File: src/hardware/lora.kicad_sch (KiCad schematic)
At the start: 19 parts, among them IC1 LLCC68IMLTRT, U21 TPS22916BYFPR, U22 0900FM15K0039001E, U23 BGS12WN6E6327XTSA1, Y4 NSC5359C-32M

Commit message: Changed footprints from 0603 to 0402
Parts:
- C57, C58, C59, C60, C61, C62, C63, C64, C65: footprint Capacitor_SMD:C_0603_1608Metric -> Capacitor_SMD:C_0504_1310Metric
- R32, R33: footprint Resistor_SMD:R_0603_1608Metric -> Resistor_SMD:R_0402_1005Metric
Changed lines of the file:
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@@
 			)
 		)
-		(property "Footprint" "Capacitor_SMD:C_0603_1608Metric"
+		(property "Footprint" "Capacitor_SMD:C_0504_1310Metric"
 			(at 136.8552 105.41 0)
 			(effects
@@
 			)
 		)
-		(property "Footprint" "Capacitor_SMD:C_0603_1608Metric"
+		(property "Footprint" "Capacitor_SMD:C_0504_1310Metric"
 			(at 104.14 67.6148 0)
 			(effects
@@
 			)
 		)
-		(property "Footprint" "Resistor_SMD:R_0603_1608Metric"
+		(property "Footprint" "Resistor_SMD:R_0402_1005Metric"
 			(at 66.548 127 90)
 			(effects
@@
 			)
 		)
-		(property "Footprint" "Capacitor_SMD:C_0603_1608Metric"
+		(property "Footprint" "Capacitor_SMD:C_0504_1310Metric"
 			(at 53.0352 128.27 0)
 			(effects
@@
 			)
 		)
-		(property "Footprint" "Capacitor_SMD:C_0603_1608Metric"
+		(property "Footprint" "Capacitor_SMD:C_0504_1310Metric"
 			(at 107.95 91.7448 0)
 			(effects
@@
 			)
 		)
-		(property "Footprint" "Resistor_SMD:R_0603_1608Metric"
+		(property "Footprint" "Resistor_SMD:R_0402_1005Metric"
 			(at 115.57 70.358 90)
 			(effects
@@
 			)
 		)
-		(property "Footprint" "Capacitor_SMD:C_0603_1608Metric"
+		(property "Footprint" "Capacitor_SMD:C_0504_1310Metric"
 			(at 225.0948 116.84 0)
 			(effects
@@
 			)
 		)
-		(property "Footprint" "Capacitor_SMD:C_0603_1608Metric"
+		(property "Footprint" "Capacitor_SMD:C_0504_1310Metric"
 			(at 105.1052 66.04 0)
 			(effects
@@
 			)
 		)
-		(property "Footprint" "Capacitor_SMD:C_0603_1608Metric"
+		(property "Footprint" "Capacitor_SMD:C_0504_1310Metric"
 			(at 125.4252 105.41 0)
 			(effects
@@
 			)
 		)
-		(property "Footprint" "Capacitor_SMD:C_0603_1608Metric"
+		(property "Footprint" "Capacitor_SMD:C_0504_1310Metric"
 			(at 234.95 129.8448 0)
 			(effects
@@
 			)
 		)
-		(property "Footprint" "Capacitor_SMD:C_0603_1608Metric"
+		(property "Footprint" "Capacitor_SMD:C_0504_1310Metric"
 			(at 49.8348 109.22 0)
 			(effects

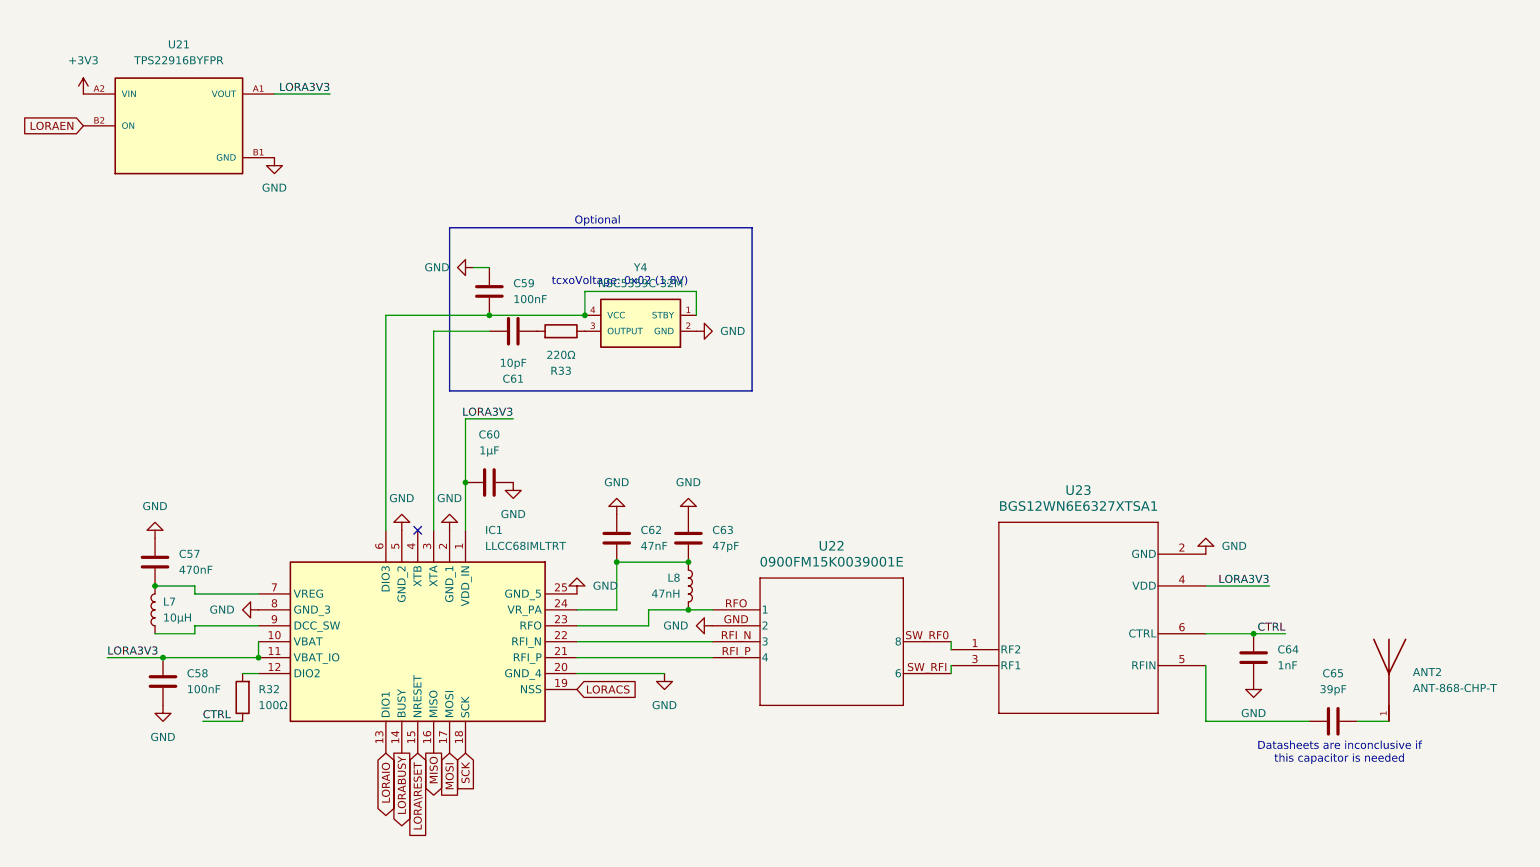
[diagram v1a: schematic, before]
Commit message: Replaced global labels with pin headers
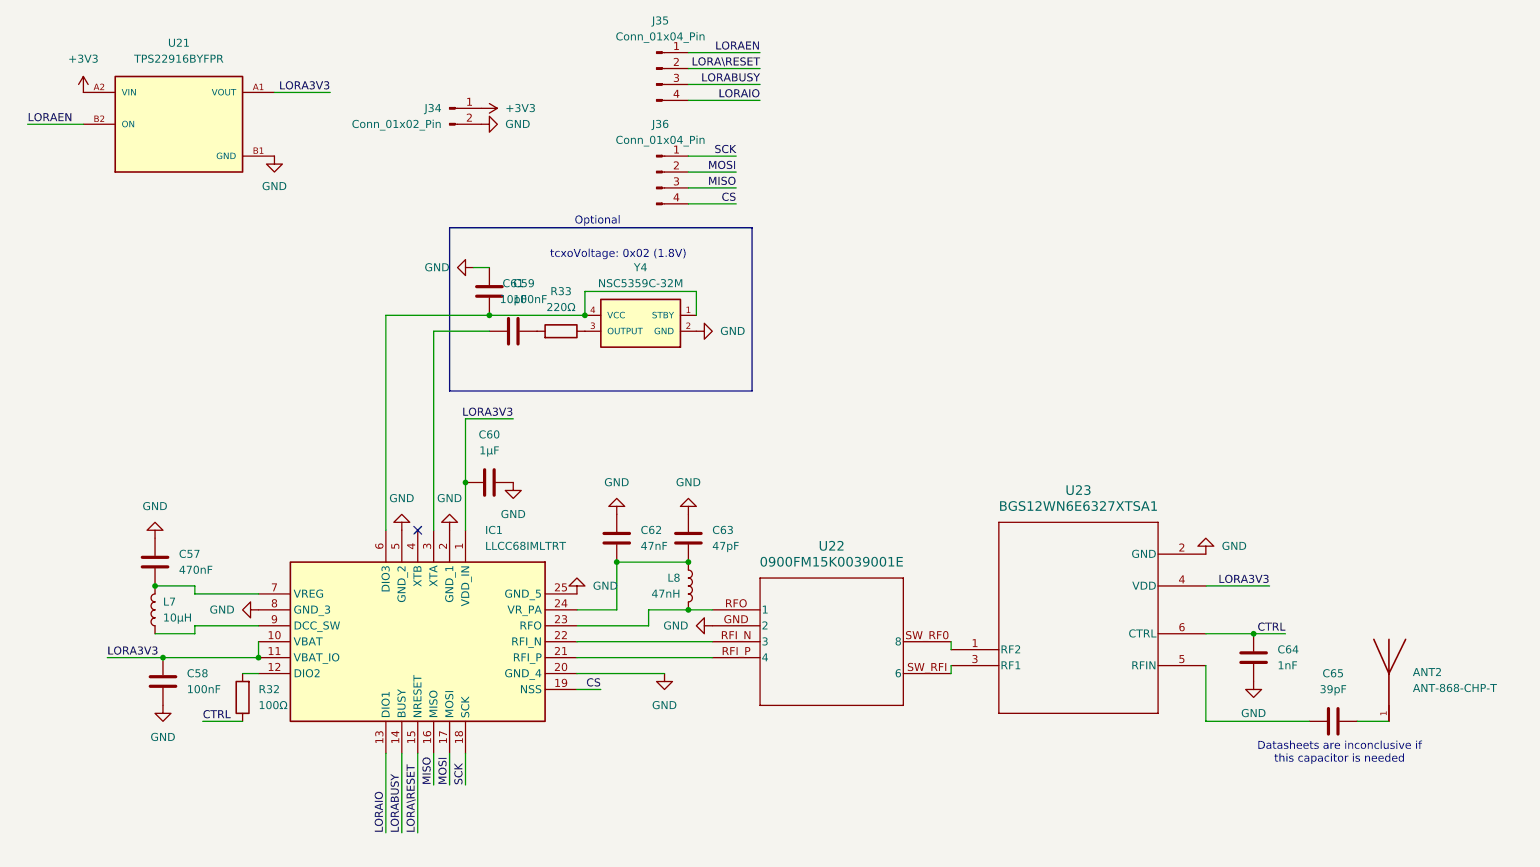
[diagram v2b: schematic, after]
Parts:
- added J34: Conn_01x02_Pin, symbol Connector:Conn_01x02_Pin
- added J35, J36: Conn_01x04_Pin, symbol Connector:Conn_01x04_Pin
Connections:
- net +3V3: now also J34.1 (Pin_1)
- net GND: now also J34.2 (Pin_2)
- net LORABUSY: now also J35.3 (Pin_3)
- net LORAEN: now also J35.1 (Pin_1)
- net LORAIO: now also J35.4 (Pin_4)
- net LORA\RESET: now also J35.2 (Pin_2)
- net MISO: now also J36.3 (Pin_3)
- net MOSI: now also J36.2 (Pin_2)
- net SCK: now also J36.1 (Pin_1)
- net LORACS renamed CS
- net CS: now also J36.4 (Pin_4)

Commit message: Reannotated schematic
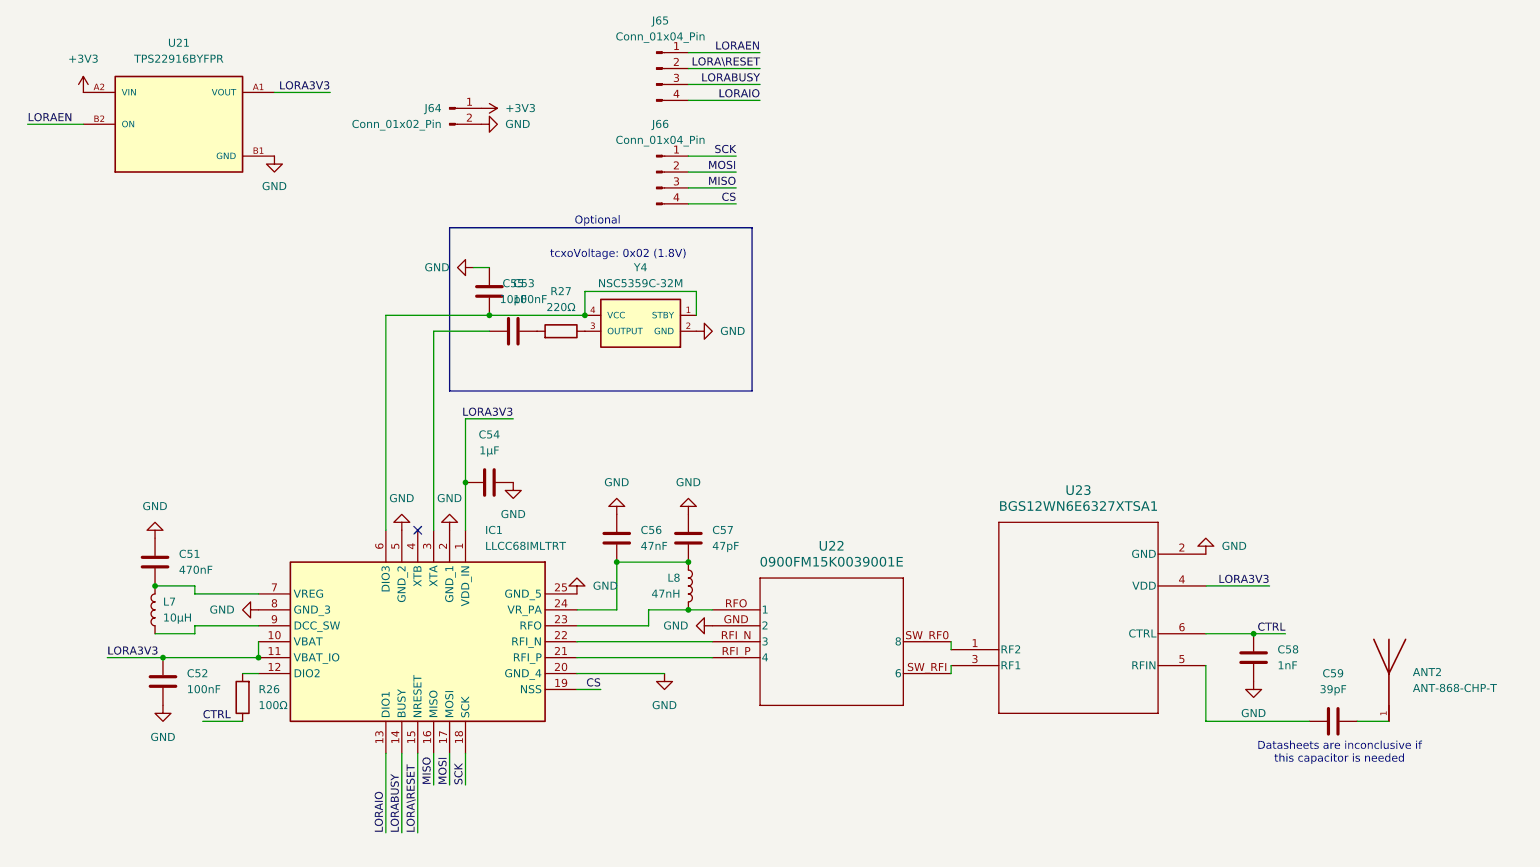
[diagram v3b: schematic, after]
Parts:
- renumbered C57 to C51, C58 to C52, C59 to C53, C60 to C54, C61 to C55, C62 to C56, C63 to C57, C64 to C58, C65 to C59, J34 to J64, J35 to J65, J36 to J66, R32 to R26, R33 to R27

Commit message: Assigned pin header footprints
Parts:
- J64: footprint (none) -> Connector_PinHeader_2.54mm:PinHeader_1x02_P2.54mm_Horizontal
- J65, J66: footprint (none) -> Connector_PinHeader_2.54mm:PinHeader_1x04_P2.54mm_Horizontal
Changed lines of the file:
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@@
 			)
 		)
-		(property "Footprint" ""
+		(property "Footprint" "Connector_PinHeader_2.54mm:PinHeader_1x04_P2.54mm_Horizontal"
 			(at 130.81 43.18 0)
 			(effects
@@
 			)
 		)
-		(property "Footprint" ""
+		(property "Footprint" "Connector_PinHeader_2.54mm:PinHeader_1x04_P2.54mm_Horizontal"
 			(at 130.81 26.67 0)
 			(effects
@@
 			)
 		)
-		(property "Footprint" ""
+		(property "Footprint" "Connector_PinHeader_2.54mm:PinHeader_1x02_P2.54mm_Horizontal"
 			(at 97.79 33.02 0)
 			(effects

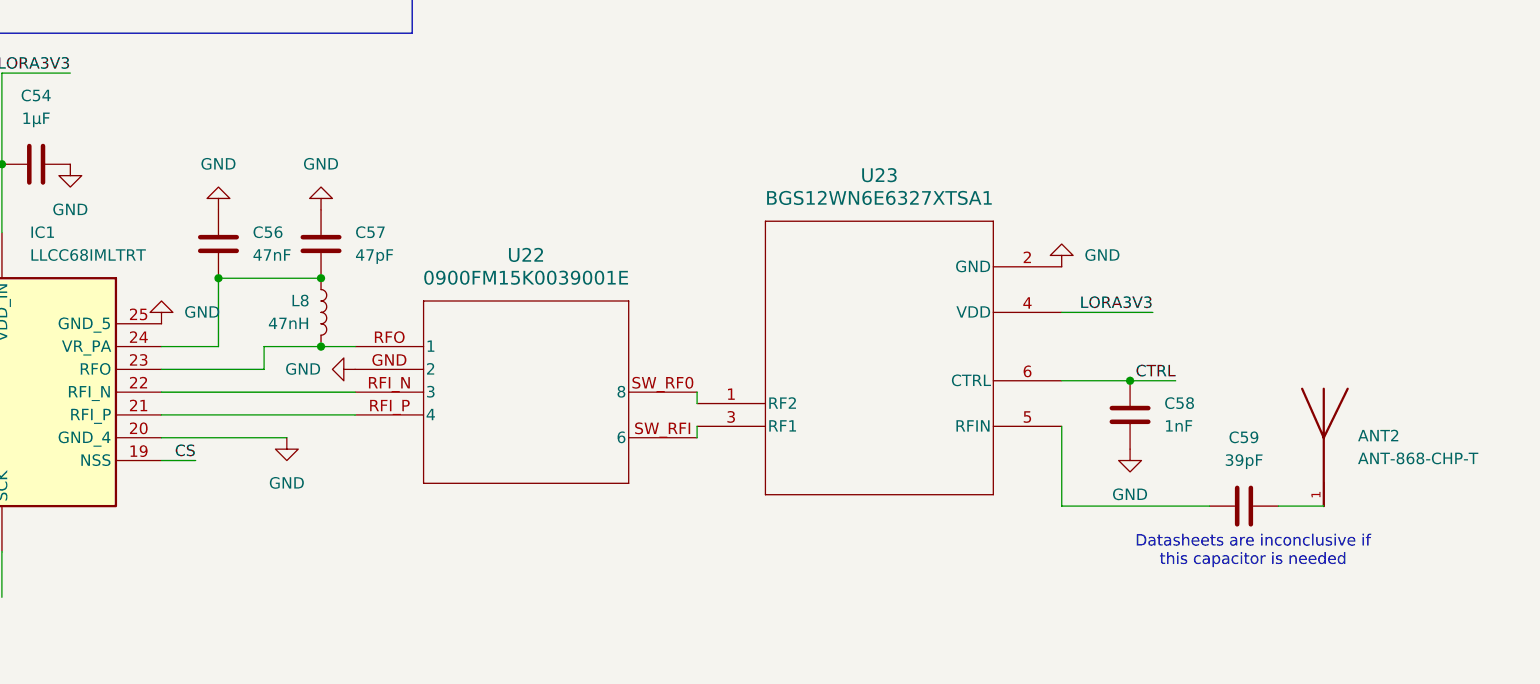
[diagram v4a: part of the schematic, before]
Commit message: Fixed 0900FM15K0039001E symbol
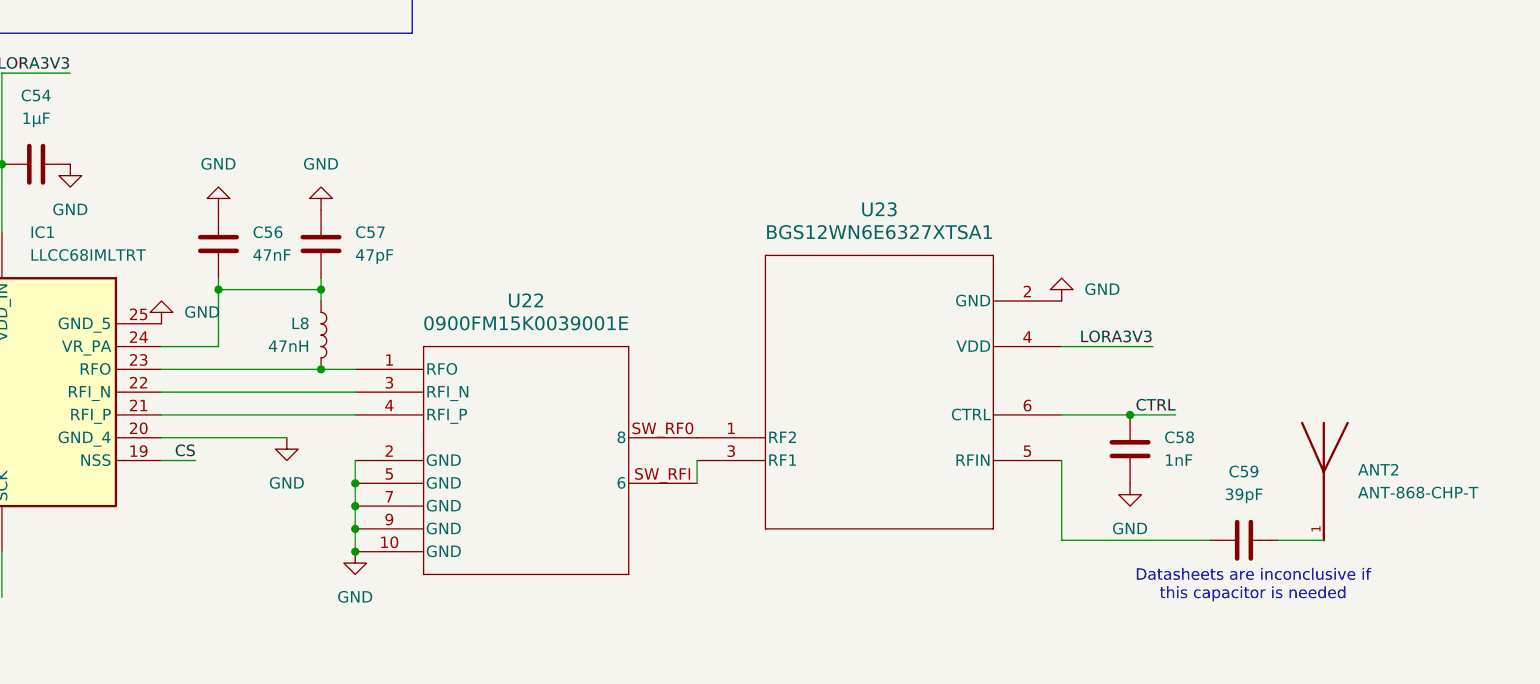
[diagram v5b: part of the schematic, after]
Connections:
- net GND: now also U22.10 (GND), U22.2 (GND), U22.5 (GND), U22.7 (GND), U22.9 (GND); no longer U22.GND (2)
- net at IC1.22 (RFI_N): now also U22.3 (RFI_N); no longer U22.RFI_N (3)
- net at IC1.21 (RFI_P): now also U22.4 (RFI_P); no longer U22.RFI_P (4)
- net at IC1.23 (RFO), L8.2: now also U22.1 (RFO); no longer U22.RFO (1)
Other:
- moved on the sheet: ANT2, C58, C59, L8, U23

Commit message: Fixed 0900FM15K0039001E symbol
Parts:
- U22: footprint Project:QFP20P0X0X31-0_JOT -> QFP20P0X0X31-0_JOT
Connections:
- net at U23.1 (RF2): now also U22.8 (SW_RFO); no longer U22.SW_RF0 (8)
- net at U23.3 (RF1): now also U22.6 (SW_RFI); no longer U22.SW_RFI (6)
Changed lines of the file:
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@@
-	(wire
-		(pts
-			(xy 177.8 128.27) (xy 177.8 125.73)
-		)
-		(stroke
-			(width 0)
-			(type default)
-		)
-	)
 	(wire
 		(pts
@@
 			)
 		)
-		(property "Footprint" "Project:QFP20P0X0X31-0_JOT"
+		(property "Footprint" "QFP20P0X0X31-0_JOT"
 			(at 139.7 118.11 0)
 			(effects
@@
 		(pin "3"
 		)
-		(pin "SW_RF0"
+		(pin "8"
 		)
 		(pin "4"
@@
 		(pin "2"
 		)
-		(pin "SW_RFI"
+		(pin "6"
 		)
 		(pin "9"

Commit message: Fixed ANT1 Footprint
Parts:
- renumbered IC1 to U?
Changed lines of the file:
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@@
 		(dnp no)
 		(fields_autoplaced yes)
-		(property "Reference" "IC1"
+		(property "Reference" "U?"
 			(at 103.4481 100.33 90)
 			(effects
@@
 			(project "raywatch"
 				(path "/7b654ee8-2a53-4d39-8b7d-32c7bb3cb0ed/500b48f3-f083-4626-a865-624bdd615c7c"
-					(reference "IC1")
+					(reference "U?")
 					(unit 1)
 				)

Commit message: Fixed ANT2
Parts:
- ANT2: footprint Project:XTAL_ABS07-32.768KHZ-7-T -> ANT-868-CHP-T:XDCR_ANT-868-CHP-T
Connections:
- net GND: now also ANT2.2 (GND)
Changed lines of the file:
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@@
+	)
+	(symbol
+		(lib_id "power:GND")
+		(at 247.65 113.03 180)
+		(unit 1)
+		(exclude_from_sim no)
+		(in_bom yes)
+		(on_board yes)
+		(dnp no)
+		(fields_autoplaced yes)
+		(property "Reference" "#PWR0497"
+			(at 247.65 106.68 0)
+			(effects
+				(font
+					(size 1.27 1.27)
+				)
+				(hide yes)
+			)
+		)
+		(property "Value" "GND"
+			(at 247.65 107.95 0)
+			(effects
+				(font
+					(size 1.27 1.27)
+				)
+			)
+		)
+		(property "Footprint" ""
+			(at 247.65 113.03 0)
+			(effects
+				(font
+					(size 1.27 1.27)
+				)
+				(hide yes)
+			)
+		)
+		(property "Datasheet" ""
+			(at 247.65 113.03 0)
+			(effects
+				(font
+					(size 1.27 1.27)
+				)
+				(hide yes)
+			)
+		)
+		(property "Description" "Power symbol creates a global label with name \"GND\" , ground"
+			(at 247.65 113.03 0)
+			(effects
+				(font
+					(size 1.27 1.27)
+				)
+				(hide yes)
+			)
+		)
+		(pin "1"
+		)
+		(instances
+			(project "raywatch"
+				(path "/7b654ee8-2a53-4d39-8b7d-32c7bb3cb0ed/500b48f3-f083-4626-a865-624bdd615c7c"
+					(reference "#PWR0497")
+					(unit 1)
+				)
+			)
+		)
 	)
 	(symbol
@@
 			)
 		)
-		(property "Footprint" "Project:XTAL_ABS07-32.768KHZ-7-T"
+		(property "Footprint" "ANT-868-CHP-T:XDCR_ANT-868-CHP-T"
 			(at 247.65 129.54 0)
 			(effects
@@
 		(pin "1"
 		)
-		(instances
+		(pin "2"
+		)
+		(instances
